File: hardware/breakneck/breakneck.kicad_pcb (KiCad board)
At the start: 2 copper layers, 53.3 x 64 mm, 82 parts, among them J1 CONN_EAST, J10 CONN_WEST, J2 GS2, J3 CONN_01X02, J4 GS3, J5 USB_C_Receptacle, J6 GS3, J7 CONN_OLED, J8 CONN_SOUTH, J9 CONN_JTAG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

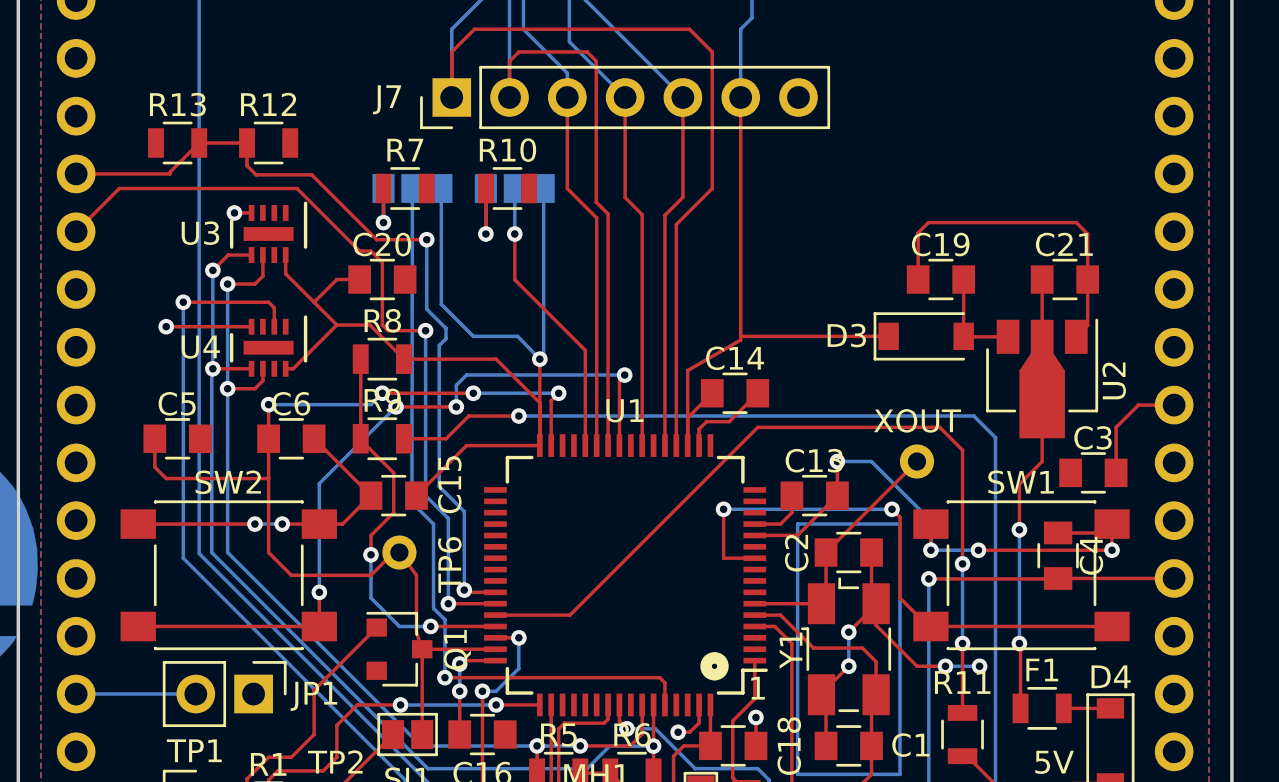
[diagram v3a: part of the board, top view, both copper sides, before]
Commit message: Moved C3 from under SW1, removed redundant SW traces, and aligned vias.
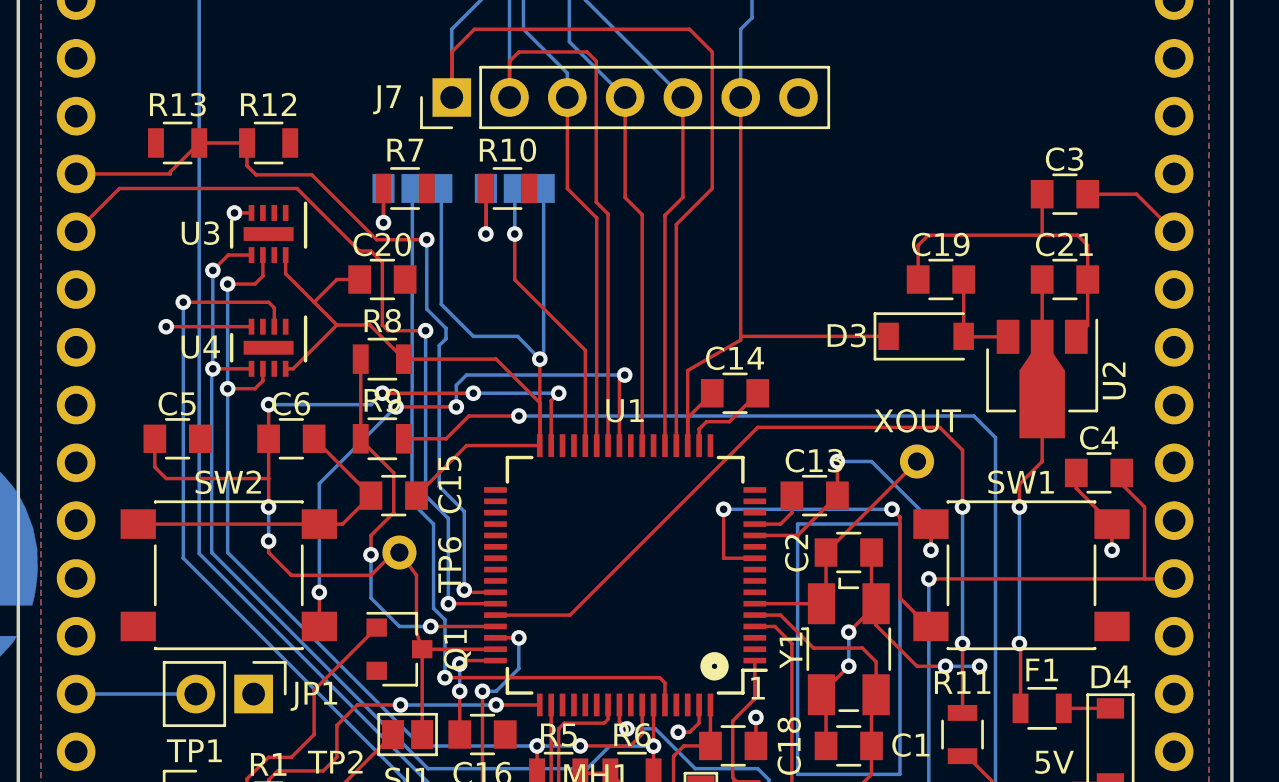
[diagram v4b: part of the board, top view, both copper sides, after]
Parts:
- moved C3 12.3 mm to (146.0, 88.2)
- moved C4 4.06 mm to (147.5, 100.5), turned to 0 degrees
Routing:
- net Net-(SW2-Pad2): track 33.4 -> 25.4 mm
- net Net-(SW1-Pad2): track 24.8 -> 16.8 mm
- net GND: track 138.0 -> 131.2 mm, vias 19 -> 16
- net Net-(C4-Pad2): track 37.5 -> 42.6 mm
- net /VCORE: vias 4 -> 6

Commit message: Connected 32KHz crystal, RTC, and tamper pins for timing attacks, and added a solder bridge jumper to support a suitable ground bridge when not in use (unfortunately causing massive net and schematic changes.
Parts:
- added J11: GS2, Connectors:GS2, B.Cu at (148.0, 113.4)
- moved C7 3.10 mm to (143.0, 78.0), turned to 270 degrees
- moved D+ 1.02 mm to (138.3, 116.0)
- moved XIN 1.00 mm to (136.2, 116.0)
- moved R3 0.55 mm to (134.0, 116.0)
- moved D4 0.14 mm to (148.0, 112.6)
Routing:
- net Net-(J1-Pad19): track 0.00 -> 32.2 mm, vias 0 -> 4
- net Net-(J1-Pad18): track 0.00 -> 26.4 mm, vias 0 -> 2
- net +1V2: track 7.82 -> 11.9 mm
- net GND: track 131.2 -> 134.4 mm
- net Net-(R3-Pad1): track 8.49 -> 11.4 mm, vias 0 -> 2
- net (no net): track 31.0 -> 29.8 mm
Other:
- board text added: "Cut on J11 for 32K TA"

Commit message: Resolved false no connects in internally connected switches, by hacking.
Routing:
- net GND: track 134.4 -> 135.7 mm
- net Net-(J1-Pad19): track 32.2 -> 31.0 mm
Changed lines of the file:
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@@
 (kicad_pcb (version 4) (host pcbnew 4.0.7)
   (general
-    (links 252)
-    (no_connects 82)
+    (links 250)
+    (no_connects 80)
     (area 99.924999 63.924999 153.415001 128.075001)
     (thickness 1.6)
@@
     (mod_text_size 1 1)
     (mod_text_width 0.15)
-    (pad_size 0.6 0.6)
-    (pad_drill 0.5)
+    (pad_size 1.55 1.3)
+    (pad_drill 0)
     (pad_to_mask_clearance 0.0508)
     (aux_axis_origin 0 0)
@@
     (pad 1 smd rect (at 3.98 -2.25) (size 1.55 1.3) (layers F.Cu F.Paste F.Mask)
       (net 2 GND))
-    (pad 2 smd rect (at 3.98 2.25) (size 1.55 1.3) (layers F.Cu F.Paste F.Mask)
-      (net 83 "Net-(SW1-Pad2)"))
+    (pad 2 smd rect (at 3.98 2.25) (size 1.55 1.3) (layers F.Cu F.Paste F.Mask))
     (model ${KIPRJMOD}/modules/packages3d/Buttons_Switches_SMD.3dshapes/SW_SPST_PTS645.wrl
       (at (xyz 0 0 0))
@@
     (fp_line (start -3.23 3.23) (end 3.23 3.23) (layer F.SilkS) (width 0.12))
     (fp_circle (center 0 0) (end 1.75 -0.05) (layer F.Fab) (width 0.1))
-    (pad 2 smd rect (at -3.98 2.25) (size 1.55 1.3) (layers F.Cu F.Paste F.Mask)
-      (net 84 "Net-(SW2-Pad2)"))
+    (pad 2 smd rect (at -3.98 2.25) (size 1.55 1.3) (layers F.Cu F.Paste F.Mask))
     (pad 1 smd rect (at -3.98 -2.25) (size 1.55 1.3) (layers F.Cu F.Paste F.Mask)
       (net 2 GND))
@@
   (segment (start 130.52 68.64) (end 131.16 68) (width 0.1524) (layer B.Cu) (net 2))
   (segment (start 117.22 71) (end 117.22 72.08) (width 0.1524) (layer B.Cu) (net 2) (status 30))
+  (segment (start 148 114.04) (end 148 112.76) (width 1) (layer B.Cu) (net 2))
   (segment (start 139.5 100) (end 135.5 104) (width 0.1524) (layer F.Cu) (net 3) (status 10))
   (segment (start 135.5 104) (end 135.5 106.05) (width 0.1524) (layer F.Cu) (net 3) (status 30))
@@
   (segment (start 137.25 114.9) (end 138.5 114.9) (width 0.1524) (layer F.Cu) (net 41))
   (segment (start 143.7 113.3) (end 148.8 113.3) (width 0.1524) (layer F.Cu) (net 41))
-  (segment (start 148 114.04) (end 148 112.76) (width 1) (layer B.Cu) (net 42) (status C00000))
   (segment (start 148 114.04) (end 148 116) (width 0.1524) (layer B.Cu) (net 42))
   (segment (start 143.2 111.8) (end 143.8 112.4) (width 0.1524) (layer F.Cu) (net 42))

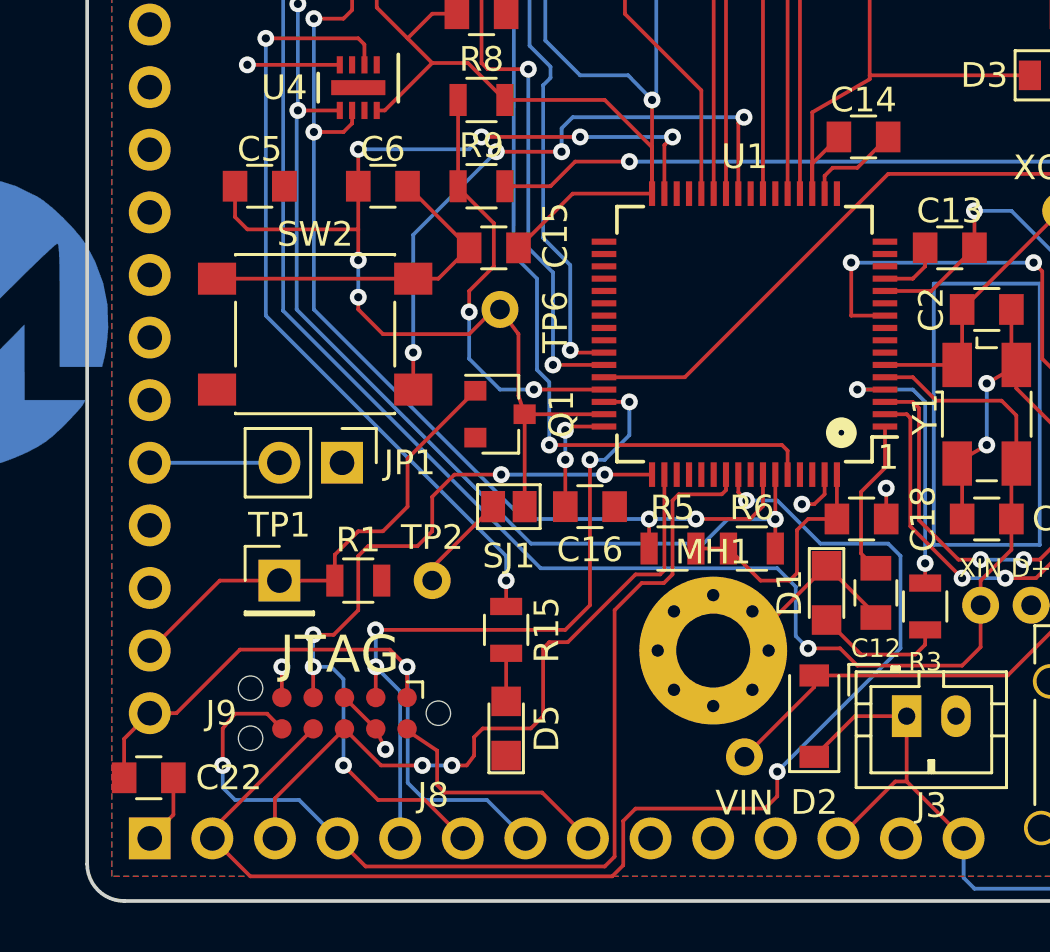
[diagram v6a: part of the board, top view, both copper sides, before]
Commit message: Resolved unconnected bootloader and reset pins, and improved 3V3 and GND.
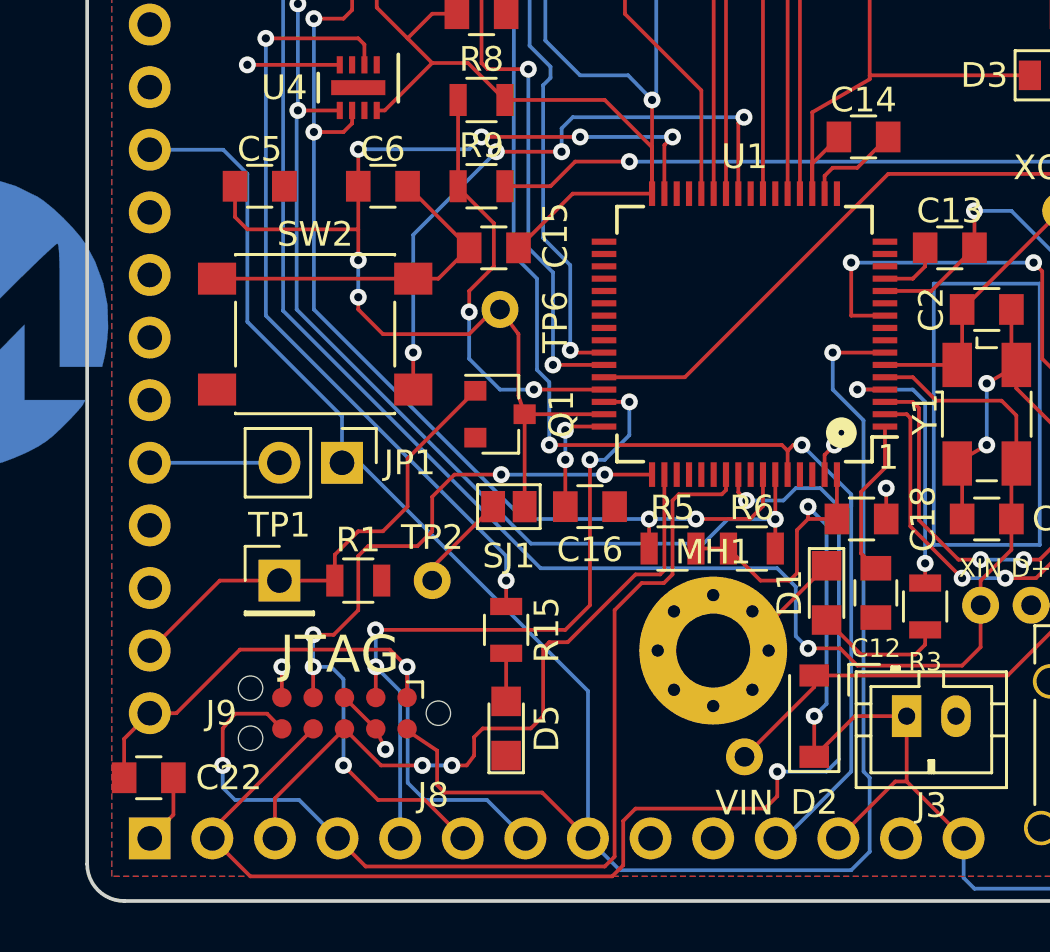
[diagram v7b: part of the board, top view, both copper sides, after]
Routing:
- net /RESET: track 9.95 -> 82.7 mm, vias 0 -> 1
- net /BLOAD: track 32.8 -> 52.3 mm, vias 1 -> 2
- net +3V3: track 173.8 -> 185.0 mm, vias 6 -> 8
- net GND: track 135.7 -> 132.4 mm
- net /JTAG_TRST: track 52.3 -> 51.5 mm

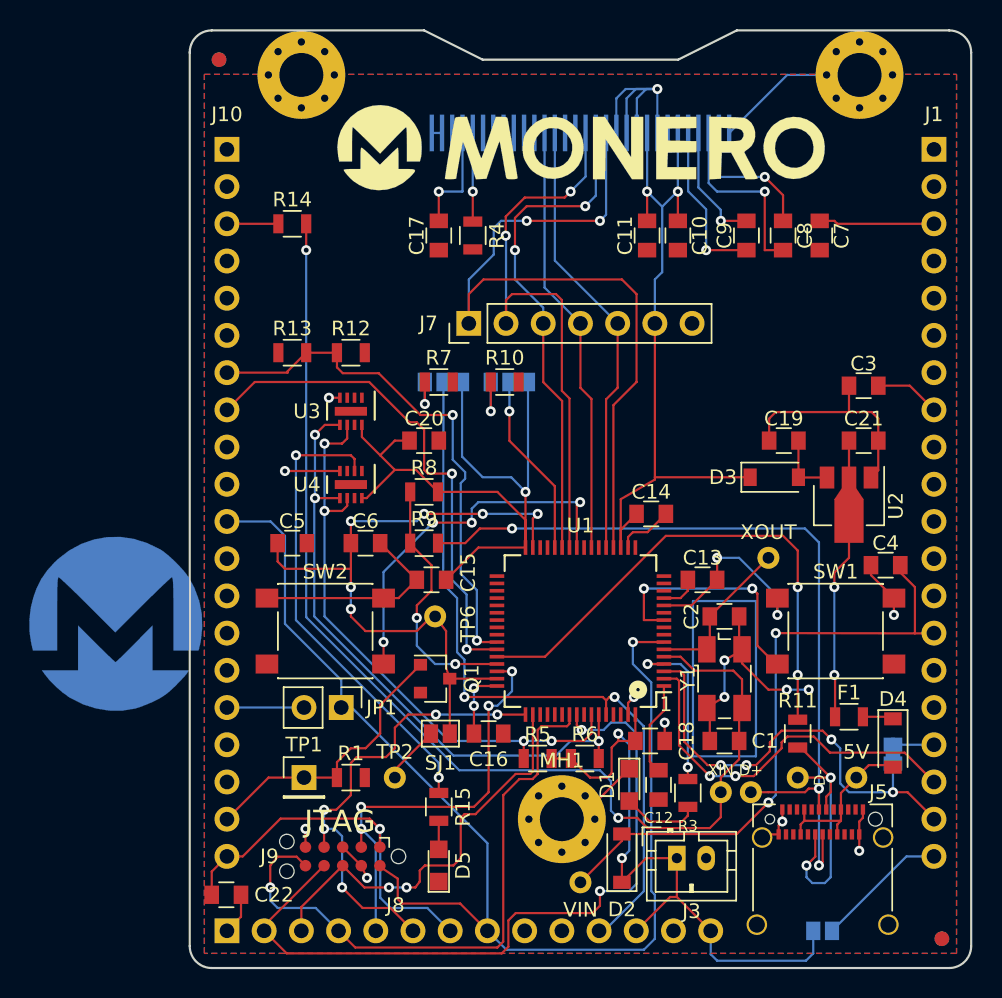
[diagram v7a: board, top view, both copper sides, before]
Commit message: Replaced copper masked logo in the least problematic place found.
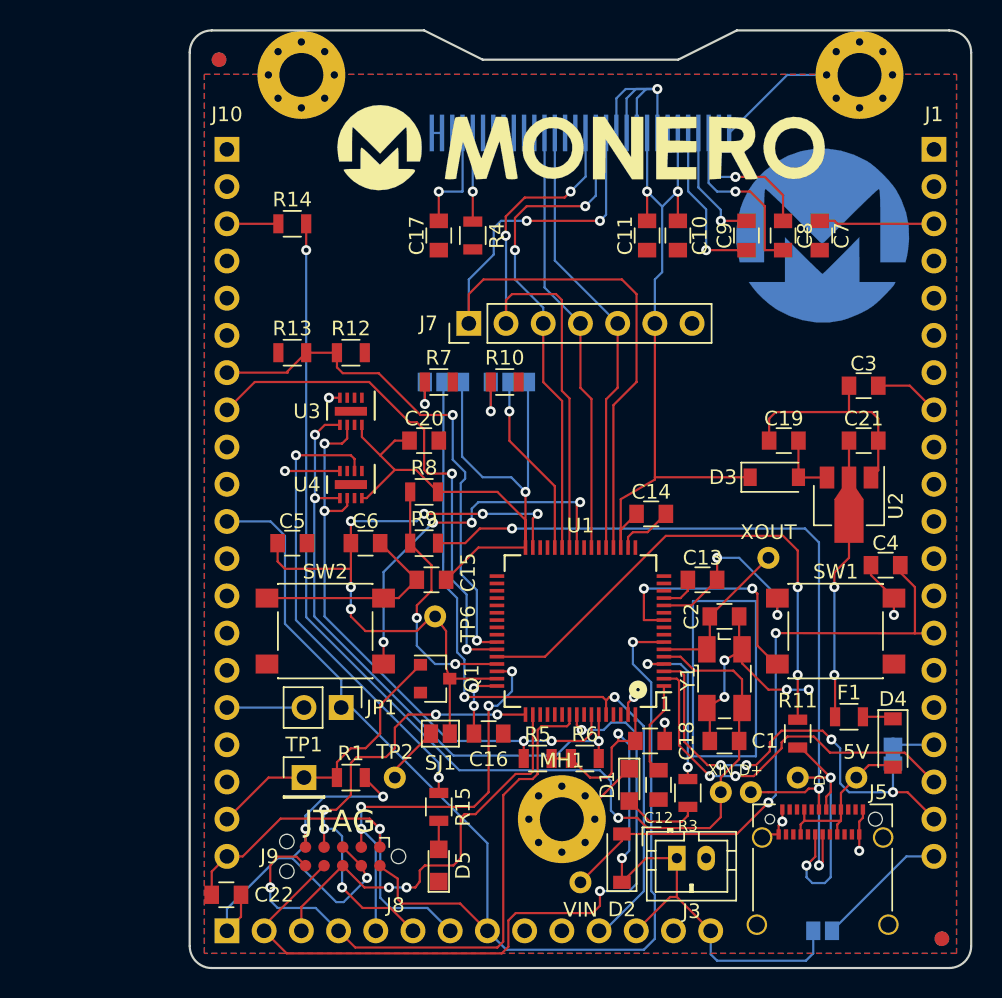
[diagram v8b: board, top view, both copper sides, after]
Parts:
- moved LOGO1 55.0 mm to (143.2, 78.0)
- moved G*** 3.75 mm to (123.0, 78.0)
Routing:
- net GND: track 132.4 -> 157.7 mm, vias 16 -> 17
- net Net-(C8-Pad2): track 12.7 -> 12.2 mm
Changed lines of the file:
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@@
   (general
     (links 250)
-    (no_connects 76)
+    (no_connects 73)
     (area 99.924999 63.924999 153.415001 128.075001)
     (thickness 1.6)
     (drawings 61)
-    (tracks 756)
+    (tracks 774)
     (zones 0)
     (modules 83)
@@
   )
   (module Monero_Logos:MoneroTextSilk (layer B.Cu)
-    (at 126.75 78 180)
+    (at 123 78 180)
     (fp_text reference G*** (at 0 0 180) (layer B.SilkS) hide
       (effects (font (thickness 0.3)) (justify mirror))
@@
   )
   (module Monero_Logos:MoneroCircleCombi (layer B.Cu)
-    (at 95 104.5 180)
+    (at 143.25 78 180)
     (fp_text reference LOGO1 (at 0 0 180) (layer B.SilkS) hide
       (effects (font (thickness 0.3)) (justify mirror))
@@
   (segment (start 134.45 107.7) (end 137.1 107.7) (width 0.1524) (layer F.Cu) (net 1))
   (segment (start 133.5 106.75) (end 134.45 107.7) (width 0.1524) (layer F.Cu) (net 1))
+  (segment (start 107.9 118.5) (end 107.9 117.6) (width 0.1524) (layer B.Cu) (net 2))
+  (segment (start 113.2 116.3) (end 111.95 115.05) (width 0.1524) (layer F.Cu) (net 2))
+  (via (at 113.2 116.3) (size 0.6858) (drill 0.3302) (layers F.Cu B.Cu) (net 2))
+  (segment (start 109.2 116.3) (end 113.2 116.3) (width 0.1524) (layer B.Cu) (net 2))
+  (segment (start 107.9 117.6) (end 109.2 116.3) (width 0.1524) (layer B.Cu) (net 2))
+  (segment (start 111.95 115.05) (end 111.95 115) (width 0.1524) (layer F.Cu) (net 2))
+  (segment (start 110.5 123.5) (end 110 123.5) (width 0.1524) (layer B.Cu) (net 2))
+  (segment (start 112.1 121.9) (end 110.5 123.5) (width 0.1524) (layer B.Cu) (net 2))
+  (segment (start 111.71 121.015) (end 112.1 121.85) (width 0.1524) (layer F.Cu) (net 2))
+  (via (at 112.1 121.85) (size 0.6858) (drill 0.3302) (layers F.Cu B.Cu) (net 2))
+  (segment (start 112.1 121.85) (end 112.1 121.9) (width 0.1524) (layer B.Cu) (net 2))
+  (segment (start 110 123.5) (end 107 120.5) (width 0.1524) (layer B.Cu) (net 2))
+  (segment (start 102.54 125.46) (end 102.54 123.96) (width 0.1524) (layer B.Cu) (net 2))
+  (segment (start 102.54 123.96) (end 106 120.5) (width 0.1524) (layer B.Cu) (net 2))
+  (segment (start 106 120.5) (end 107 120.5) (width 0.1524) (layer B.Cu) (net 2))
+  (via (at 107.9 118.5) (size 0.6858) (drill 0.3302) (layers F.Cu B.Cu) (net 2))
+  (segment (start 107 120.5) (end 107.9 119.6) (width 0.1524) (layer B.Cu) (net 2))
+  (segment (start 107.9 119.6) (end 107.9 118.5) (width 0.1524) (layer B.Cu) (net 2))
+  (segment (start 107.9 118.5) (end 107.9 119.745) (width 0.1524) (layer F.Cu) (net 2))
   (segment (start 129.92 110.7) (end 129.92 109.9) (width 0.1524) (layer F.Cu) (net 2))
   (via (at 130.32 109.5) (size 0.6858) (drill 0.3302) (layers F.Cu B.Cu) (net 2))
@@
   (segment (start 114.25 102.75) (end 115.5 101.5) (width 0.1524) (layer F.Cu) (net 2))
   (segment (start 113 99) (end 115.5 101.5) (width 0.1524) (layer F.Cu) (net 2))
-  (segment (start 111.71 121.015) (end 112.1 121.85) (width 0.1524) (layer F.Cu) (net 2))
-  (via (at 112.1 121.85) (size 0.6858) (drill 0.3302) (layers F.Cu B.Cu) (net 2))
-  (segment (start 107.9 119.745) (end 107.9 118.5) (width 0.1524) (layer F.Cu) (net 2))
-  (via (at 107.9 118.5) (size 0.6858) (drill 0.3302) (layers F.Cu B.Cu) (net 2))
   (segment (start 110.44 119.745) (end 111.71 121.015) (width 0.1524) (layer F.Cu) (net 2))
   (segment (start 132 116.5) (end 132 116.4) (width 0.1524) (layer F.Cu) (net 2))
@@
   (segment (start 136.12 73.995) (end 136.12 71) (width 0.1524) (layer B.Cu) (net 8) (status 20))
   (segment (start 136.125 74) (end 136.12 73.995) (width 0.1524) (layer B.Cu) (net 8))
-  (segment (start 139.25 74) (end 136.125 74) (width 0.1524) (layer B.Cu) (net 8))
-  (via (at 139.25 74) (size 0.6858) (drill 0.3302) (layers F.Cu B.Cu) (net 8))
+  (segment (start 137.25 74) (end 136.125 74) (width 0.1524) (layer B.Cu) (net 8))
+  (via (at 137.25 74) (size 0.6858) (drill 0.3302) (layers F.Cu B.Cu) (net 8))
   (segment (start 140.5 75.25) (end 139.25 74) (width 0.1524) (layer F.Cu) (net 8))
+  (segment (start 139.25 74) (end 137.25 74) (width 0.1524) (layer F.Cu) (net 8))
   (segment (start 140.5 79) (end 139.25 79) (width 0.1524) (layer F.Cu) (net 9) (status 10))
   (segment (start 135.42 74.42) (end 135.42 71) (width 0.1524) (layer B.Cu) (net 9) (status 20))
   (segment (start 136 75) (end 135.42 74.42) (width 0.1524) (layer B.Cu) (net 9))
-  (segment (start 139.25 75) (end 136 75) (width 0.1524) (layer B.Cu) (net 9))
-  (via (at 139.25 75) (size 0.6858) (drill 0.3302) (layers F.Cu B.Cu) (net 9))
-  (segment (start 139.25 79) (end 139.25 75) (width 0.1524) (layer F.Cu) (net 9))
+  (segment (start 137.25 75) (end 136 75) (width 0.1524) (layer B.Cu) (net 9))
+  (via (at 137.25 75) (size 0.6858) (drill 0.3302) (layers F.Cu B.Cu) (net 9))
+  (segment (start 139.25 79) (end 139.25 76) (width 0.1524) (layer F.Cu) (net 9))
+  (segment (start 139.25 76) (end 138.25 75) (width 0.1524) (layer F.Cu) (net 9))
+  (segment (start 138.25 75) (end 137.25 75) (width 0.1524) (layer F.Cu) (net 9))
   (segment (start 134.72 71) (end 134.72 74.72) (width 0.1524) (layer B.Cu) (net 10) (status 10))
   (segment (start 136.25 77) (end 138 77) (width 0.1524) (layer F.Cu) (net 10) (status 20))
